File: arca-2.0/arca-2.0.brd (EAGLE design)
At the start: 304.8 x 101.6 mm, 20 parts

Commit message: drivers
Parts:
- added CON_BATTERY, CON_DRV1, CON_DRV2, CON_DRV3, CON_DRV4, CON_DRV5, CON_DRV6: LPTA-2POS, con-phoenix-5mm:8.2X2
- added D10, D5, D6, D7, D8, D9: SS54, diode-ss:SS*
- added D4: (no value), diode:DO201-15
- added DRV_STAT_1, DRV_STAT_2, DRV_STAT_3, DRV_STAT_4, DRV_STAT_5, DRV_STAT_6, FS_STAT_1, FS_STAT_2, FS_STAT_3, FS_STAT_4, FS_STAT_5, FS_STAT_6: (no value), led:CHIPLED_1206
- added FS1, FS2, FS3, FS4, FS5, FS6: 178.6165, fuse-holder-littlefuse:178.6165
- added PWR_12V: RED, led:CHIPLED_1206
- added R10, R13, R16, R19, R22, R7: 10k, rcl:R1206
- added R11, R12, R14, R15, R17, R18, R20, R21, R23, R24, R8, R9: 220, rcl:R1206
- added R6: 300, rcl:R1206
- added SW1: 1101M2S3CQE2, switch-slide:1101M2S3CQE2
- added T1, T2, T3, T4, T5, T6: FQP30N06L, transistor-FQP:TO220V
- C5: value (none) -> 10u
- R1: value 10k -> 68k
- R2: value 1.5k -> 10k
- moved C6 28.4 mm to (289.6, 52.1)
- moved R1 28.4 mm to (284.5, 43.2)
- moved C2 28.4 mm to (289.6, 10.2)
- moved C4 28.4 mm to (289.6, 27.9)
- moved D1 28.4 mm to (284.5, 16.5)
- moved C1 28.4 mm to (269.2, 11.4)
- moved C3 28.4 mm to (269.2, 29.2)
- moved C5 28.4 mm to (269.2, 53.3)
- moved D2 28.4 mm to (284.5, 34.3)
- moved D3 28.4 mm to (284.5, 58.4)
- moved PWR_10V 28.4 mm to (270.5, 59.7)
- moved PWR_3V3 28.4 mm to (270.5, 17.8)
- moved PWR_5V 28.4 mm to (270.5, 35.6)
- moved R2 28.4 mm to (284.5, 40.6)
- moved R3 28.4 mm to (264.2, 17.8)
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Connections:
- new net 12V_CON: CON_BATTERY.1, CON_BATTERY.2, SW1.2
- new net 12V_IN: D4.A, SW1.1
- new net DRV_CTL_1: R7.2, T1.1
- new net DRV_CTL_2: R10.2, T2.1
- new net DRV_CTL_3: R13.2, T3.1
- new net DRV_CTL_4: R16.2, T4.1
- new net DRV_CTL_5: R19.2, T5.1
- new net DRV_CTL_6: R22.2, T6.1
- new net DRV_NEG_1: CON_DRV1.3, CON_DRV1.4, D5.P$2, R9.1, T1.2
- new net DRV_NEG_2: CON_DRV2.3, CON_DRV2.4, D6.P$2, R12.1, T2.2
- new net DRV_NEG_3: CON_DRV3.3, CON_DRV3.4, D7.P$2, R15.1, T3.2
- new net DRV_NEG_4: CON_DRV4.3, CON_DRV4.4, D8.P$2, R18.1, T4.2
- new net DRV_NEG_5: CON_DRV5.3, CON_DRV5.4, D9.P$2, R21.1, T5.2
- new net DRV_NEG_6: CON_DRV6.3, CON_DRV6.4, D10.P$2, R24.1, T6.2
- new net DRV_POS_1: CON_DRV1.1, CON_DRV1.2, D5.P$1, DRV_STAT_1.A, FS1.1, FS1.2, FS1.3, FS1.4, FS_STAT_1.A
- new net DRV_POS_2: CON_DRV2.1, CON_DRV2.2, D6.P$1, DRV_STAT_2.A, FS2.1, FS2.2, FS2.3, FS2.4, FS_STAT_2.A
- new net DRV_POS_3: CON_DRV3.1, CON_DRV3.2, D7.P$1, DRV_STAT_3.A, FS3.1, FS3.2, FS3.3, FS3.4, FS_STAT_3.A
- new net DRV_POS_4: CON_DRV4.1, CON_DRV4.2, D8.P$1, DRV_STAT_4.A, FS4.1, FS4.2, FS4.3, FS4.4, FS_STAT_4.A
- new net DRV_POS_5: CON_DRV5.1, CON_DRV5.2, D9.P$1, DRV_STAT_5.A, FS5.1, FS5.2, FS5.3, FS5.4, FS_STAT_5.A
- new net DRV_POS_6: CON_DRV6.1, CON_DRV6.2, D10.P$1, DRV_STAT_6.A, FS6.1, FS6.2, FS6.3, FS6.4, FS_STAT_6.A
- new net N$1: FS_STAT_2.C, R11.2
- new net N$10: DRV_STAT_3.C, R15.2
- new net N$11: FS_STAT_4.C, R17.2
- new net N$12: DRV_STAT_4.C, R18.2
- new net N$13: FS_STAT_5.C, R20.2
- new net N$14: DRV_STAT_5.C, R21.2
- new net N$15: FS_STAT_6.C, R23.2
- new net N$16: DRV_STAT_6.C, R24.2
- new net N$5: PWR_12V.C, R6.2
- new net N$6: DRV_STAT_2.C, R12.2
- new net N$7: FS_STAT_3.C, R14.2
- new net N$8: FS_STAT_1.C, R8.2
- new net N$9: DRV_STAT_1.C, R9.2
- net +12V: now also D4.C, FS1.5, FS1.6, FS1.7, FS1.8, FS2.5, FS2.6, FS2.7, FS2.8, FS3.5, FS3.6, FS3.7, FS3.8, FS4.5, FS4.6, FS4.7, FS4.8, FS5.5, FS5.6, FS5.7, FS5.8, FS6.5, FS6.6, FS6.7, FS6.8, PWR_12V.A
- net GND: now also CON_BATTERY.3, CON_BATTERY.4, R10.1, R11.1, R13.1, R14.1, R16.1, R17.1, R19.1, R20.1, R22.1, R23.1, R6.1, R7.1, R8.1, T1.3, T2.3, T3.3, T4.3, T5.3, T6.3
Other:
- board text added: "+"
- board text added: "+12V"
- board text added: "-"
- board text added: "GND"

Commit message: started on LC work
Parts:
- added C10, C7, C8, C9: 1u, rcl:C1206
- added C11: 0.1u, rcl:C1206
- added C12, C13, C14, C15: 1n, rcl:C1206
- added CON_LC1, CON_LC2, CON_LC3, CON_LC4: LPTA-4POS, con-phoenix-5mm:8.2X4
- added IC1, IC2, IC3, IC4: MCP6N11R, inamp-microchip:SO-8
- added IC5: LM324D, linear:SO14
- added R25, R29: 39k, rcl:R1206
- added R26, R30: 10k, rcl:R1206
- added R27, R28, R31, R32: 62k, rcl:R1206
- added RF1, RF2, RF3, RF4, RG1, RG2, RG3, RG4: (no value), rcl:R1206
- added RZ1, RZ2, RZ3, RZ4: (no value), pot:S64W
- C6: value (none) -> 10u
- moved D8 240.5 mm to (209.6, 87.6), turned to 270 degrees
- moved R19 239.9 mm to (201.9, 68.6), turned to 180 degrees
- moved R20 229.1 mm to (175.3, 91.4), turned to 270 degrees
- moved R16 229.0 mm to (228.6, 68.6), turned to 180 degrees
- moved R21 227.3 mm to (177.8, 91.4), turned to 270 degrees
- moved T4 223.1 mm to (219.7, 71.1), turned to 90 degrees
- moved DRV_STAT_4 222.1 mm to (204.5, 83.8)
- moved FS4 218.7 mm to (214.6, 67.3), turned to 270 degrees
- moved R17 216.7 mm to (201.9, 90.2), turned to 270 degrees
- moved D9 214.9 mm to (182.9, 87.6), turned to 270 degrees
- moved R18 214.9 mm to (204.5, 90.2), turned to 270 degrees
- moved CON_DRV4 211.9 mm to (217.2, 87.6), turned to 90 degrees
- moved FS_STAT_5 210.4 mm to (175.3, 85.1)
- moved CON_DRV5 208.7 mm to (190.5, 87.6), turned to 90 degrees
- moved R22 206.4 mm to (175.3, 68.6), turned to 180 degrees
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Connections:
- new net LC1+: CON_LC1.3, CON_LC1.4, IC1.3
- new net LC1-: CON_LC1.5, CON_LC1.6, IC1.2
- new net LC1_CAL: C12.2, IC5.1, R25.2
- new net LC1_PREC: IC1.6, R28.1
- new net LC2+: CON_LC2.3, CON_LC2.4, IC2.3
- new net LC2-: CON_LC2.5, CON_LC2.6, IC2.2
- new net LC2_CAL: C14.2, R29.2
- new net LC2_PREC: IC2.6, R32.1
- new net LC3+: CON_LC3.3, CON_LC3.4, IC3.3
- new net LC3-: CON_LC3.5, CON_LC3.6, IC3.2
- new net LC3_PREC: IC3.6
- new net LC4+: CON_LC4.3, CON_LC4.4, IC4.3
- new net LC4-: CON_LC4.5, CON_LC4.6, IC4.2
- new net LC4_PREC: IC4.6
- new net LC_EN: IC1.8, IC2.8, IC3.8, IC4.8
- new net N$17: IC1.5, RF1.1, RG1.2
- new net N$18: IC1.1, RF1.2
- new net N$19: RG1.1, RZ1.S
- new net N$20: IC2.5, RF2.1, RG2.2
- new net N$21: IC2.1, RF2.2
- new net N$22: RG2.1, RZ2.S
- new net N$23: IC3.5, RF3.1, RG3.2
- new net N$24: IC3.1, RF3.2
- new net N$25: RG3.1, RZ3.S
- new net N$26: IC4.5, RF4.1, RG4.2
- new net N$27: IC4.1, RF4.2
- new net N$28: RG4.1, RZ4.S
- new net N$29: IC5.2, R25.1, R26.2
- new net N$30: R29.1, R30.2
- new net N$31: C13.1, IC5.3, R27.2
- new net N$32: C12.1, R27.1, R28.2
- new net N$33: C15.1, R31.2
- new net N$34: C14.1, R31.1, R32.2
- net +10V: now also CON_LC1.1, CON_LC1.2, CON_LC2.1, CON_LC2.2, CON_LC3.1, CON_LC3.2, CON_LC4.1, CON_LC4.2
- net +3V3: now also C10.1, C7.1, C8.1, C9.1, IC1.7, IC2.7, IC3.7, IC4.7, RZ1.E, RZ2.E, RZ3.E, RZ4.E
- net +5V: now also C11.1, IC5.4
- net GND: now also C10.2, C11.2, C13.2, C15.2, C7.2, C8.2, C9.2, CON_LC1.7, CON_LC1.8, CON_LC2.7, CON_LC2.8, CON_LC3.7, CON_LC3.8, CON_LC4.7, CON_LC4.8, IC1.4, IC2.4, IC3.4, IC4.4, IC5.11, R26.1, R30.1, RZ1.A, RZ2.A, RZ3.A, RZ4.A
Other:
- board size 304.8 x 101.6 mm -> 355.6 x 101.6 mm
- board text added: "+10V + - GND"

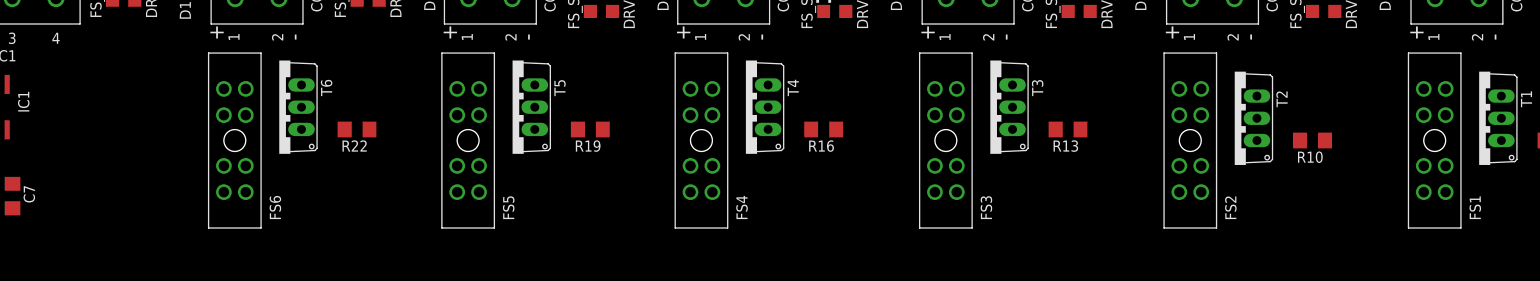
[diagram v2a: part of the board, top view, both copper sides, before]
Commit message: fixed incorrect feedback on LC inamp
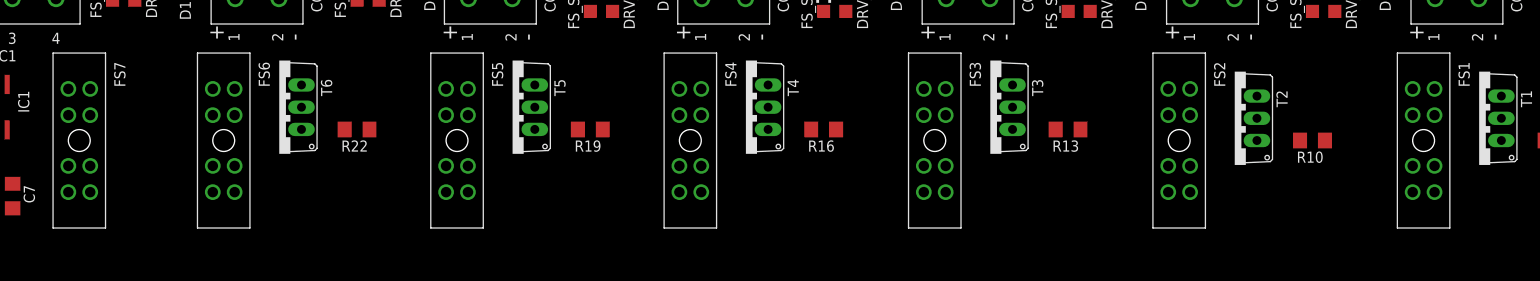
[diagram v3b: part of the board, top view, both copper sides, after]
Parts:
- added FS7: 178.6165, fuse-holder-littlefuse:178.6165
- RF1: value (none) -> 20k
- RG1: value (none) -> 200
- moved FS5 1.27 mm to (186.7, 67.3)
- moved FS1 1.27 mm to (297.2, 67.3)
- moved FS2 1.27 mm to (269.2, 67.3)
- moved FS3 1.27 mm to (241.3, 67.3)
- moved FS4 1.27 mm to (213.4, 67.3)
- moved FS6 1.27 mm to (160.0, 67.3)
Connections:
- removed net N$19: RG1.1, RZ1.S
- removed net N$20: IC2.5, RF2.1, RG2.2
- removed net N$23: IC3.5, RF3.1, RG3.2
- removed net N$26: IC4.5, RF4.1, RG4.2
- new net +10V_FS: CON_LC1.1, CON_LC1.2, CON_LC2.1, CON_LC2.2, CON_LC3.1, CON_LC3.2, CON_LC4.1, CON_LC4.2, FS7.1, FS7.2, FS7.3, FS7.4
- net +10V: now also FS7.5, FS7.6, FS7.7, FS7.8; no longer CON_LC1.1, CON_LC1.2, CON_LC2.1, CON_LC2.2, CON_LC3.1, CON_LC3.2, CON_LC4.1, CON_LC4.2
- net LC1_PREC: now also RF1.1, RG1.2
- net LC2_PREC: now also RF2.1, RG2.2
- net LC3_PREC: now also RF3.1, RG3.2
- net LC4_PREC: now also RF4.1, RG4.2
- net N$17: now also RG1.1, RZ1.S; no longer RF1.1, RG1.2
- net N$22: now also IC2.5
- net N$25: now also IC3.5
- net N$28: now also IC4.5

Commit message: rip 3.3v
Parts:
- removed C1, C2: 10u, rcl:C1206
- removed D1: SS54, diode-ss:SS*
- removed PWR_3V3: RED, led:CHIPLED_1206
- removed VR1: +3.3, LM1084:TO-263-3L
- added C16, C17, C18, C19: 1n, rcl:C1206
- added R33, R37: 39k, rcl:R1206
- added R34, R38: 10k, rcl:R1206
- added R35, R36, R39, R40: 62k, rcl:R1206
- added R41, R42, R43, R44, R45: DNP, rcl:R1206
- R27, R28: value 62k -> 56k
- R3: value 10 -> DNP
- moved R30 126.1 mm to (109.2, 47.0), turned to 270 degrees
- moved R31 118.8 mm to (111.8, 36.8), turned to 180 degrees
- moved C14 115.9 mm to (105.4, 39.4), turned to 180 degrees
- moved R32 115.7 mm to (111.8, 39.4), turned to 180 degrees
- moved C15 114.8 mm to (111.8, 34.3)
- moved R29 108.2 mm to (105.4, 41.9), turned to 180 degrees
- moved R3 53.4 mm to (312.4, 72.4)
- moved R26 21.9 mm to (109.2, 14.0), turned to 90 degrees
- moved R28 17.7 mm to (111.8, 21.6), turned to 180 degrees
- moved R27 16.6 mm to (111.8, 24.1), turned to 180 degrees
- moved C13 16.2 mm to (111.8, 26.7), turned to 0 degrees
- moved R25 13.0 mm to (105.4, 19.1), turned to 180 degrees
- moved C11 12.0 mm to (108.0, 30.5), turned to 0 degrees
- moved C12 10.2 mm to (105.4, 21.6), turned to 180 degrees
- moved IC5 5.39 mm to (100.3, 30.5), turned to 90 degrees
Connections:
- removed net LC_EN: IC1.8, IC2.8, IC3.8, IC4.8
- removed net N$2: PWR_3V3.C, R3.2
- new net LC3_CAL: C16.2, IC5.8, R33.2
- new net LC4_CAL: C18.2, IC5.14, R37.2
- new net N$19: IC5.9, R33.1, R34.2
- new net N$20: C17.1, IC5.10, R35.2
- new net N$23: C16.1, R35.1, R36.2
- new net N$26: IC5.13, R37.1, R38.2
- new net N$35: C19.1, IC5.12, R39.2
- new net N$36: C18.1, R39.1, R40.2
- net +12V: no longer C2.1, D1.P$1, VR1.P$3
- net +3V3: no longer C1.1, C10.1, C7.1, C8.1, C9.1, D1.P$2, IC1.7, IC2.7, IC3.7, IC4.7, PWR_3V3.A, VR1.P$2, VR1.P$4, VR1.P$5
- net +5V: now also C10.1, C7.1, C8.1, C9.1, IC1.7, IC1.8, IC2.7, IC2.8, IC3.7, IC3.8, IC4.7, IC4.8, R3.2, R41.2, R42.2, R43.2, R44.2, R45.2
- net DRV_CTL_1: now also R3.1
- net DRV_CTL_2: now also R41.1
- net DRV_CTL_3: now also R42.1
- net DRV_CTL_4: now also R43.1
- net DRV_CTL_5: now also R44.1
- net DRV_CTL_6: now also R45.1
- net GND: now also C17.2, C19.2, R34.1, R38.1; no longer C1.2, C2.2, R3.1, VR1.P$1
- net LC2_CAL: now also IC5.7
- net LC3_PREC: now also R36.1
- net LC4_PREC: now also R40.1
- net N$30: now also IC5.6
- net N$33: now also IC5.5

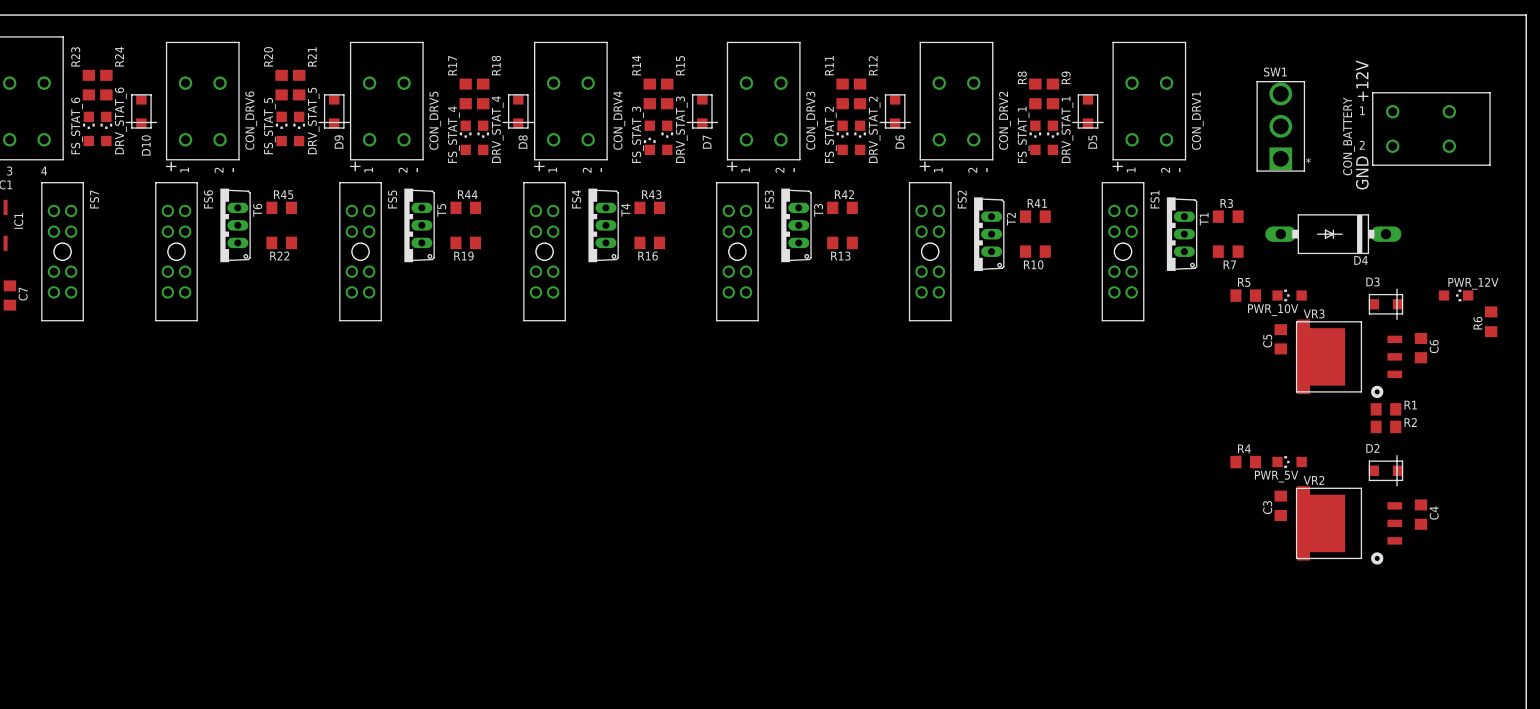
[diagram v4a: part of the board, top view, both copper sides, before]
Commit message: more compact drivers
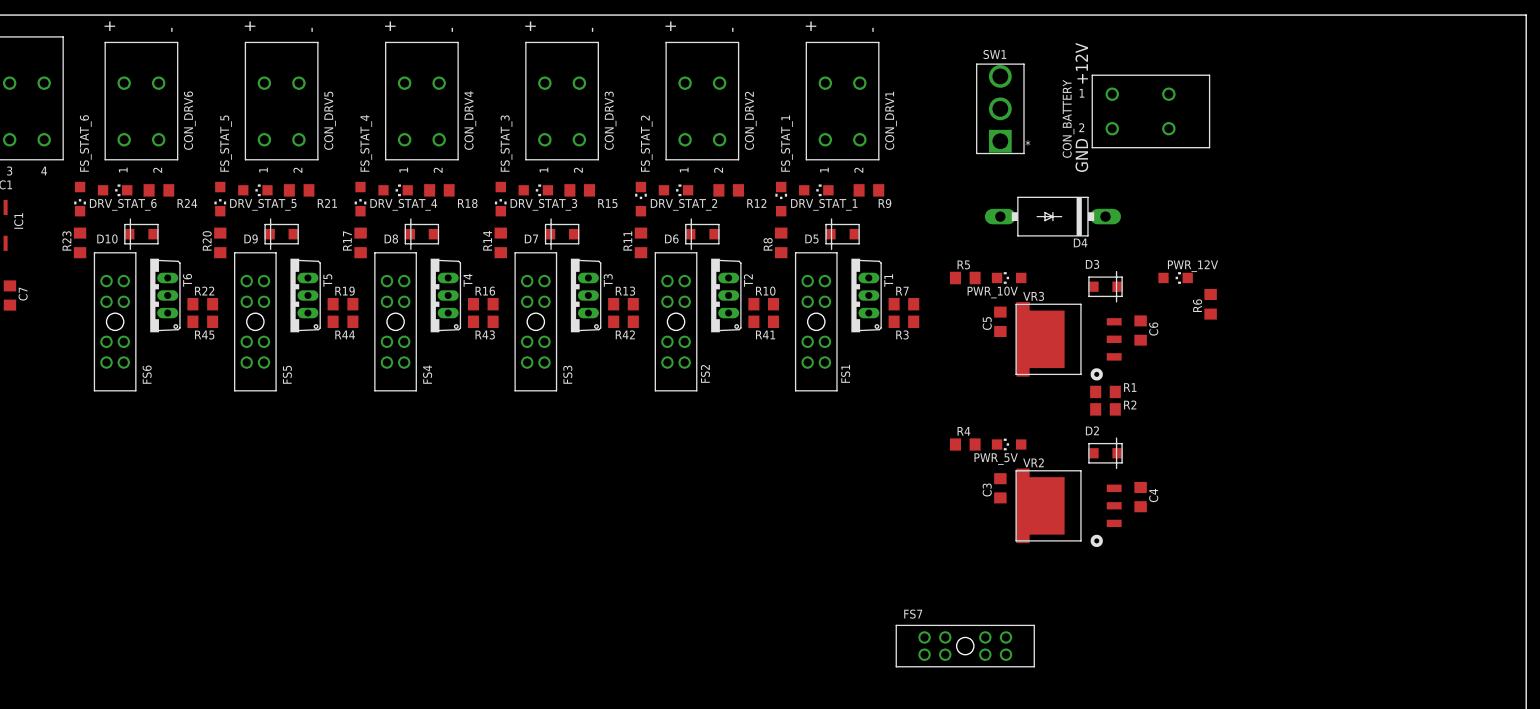
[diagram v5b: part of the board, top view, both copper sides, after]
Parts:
- moved FS7 142.7 mm to (274.3, 10.2), turned to 0 degrees
- moved R3 49.4 mm to (265.4, 57.1)
- moved R7 47.6 mm to (265.4, 59.7)
- moved T1 46.6 mm to (257.8, 61.0)
- moved FS1 45.6 mm to (252.7, 57.1)
- moved CON_DRV1 44.4 mm to (256.5, 87.6)
- moved R8 42.7 mm to (247.7, 68.6), turned to 90 degrees
- moved R41 42.2 mm to (245.1, 57.1)
- moved C3 40.7 mm to (279.4, 33.0)
- moved C5 40.7 mm to (279.4, 57.1)
- moved D4 40.7 mm to (287.0, 72.4)
- moved SW1 40.7 mm to (279.4, 92.7)
- moved C4 40.7 mm to (299.7, 31.8)
- moved C6 40.7 mm to (299.7, 55.9)
- moved CON_BATTERY 40.7 mm to (299.7, 87.6)
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
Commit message: concept for PTs
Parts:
- removed RZ1, RZ2, RZ3, RZ4: (no value), pot:S64W
- added C1, C2: (no value), rcl:C1206
- added C20: 0.1u, rcl:C1206
- added CON_PT1: LPTA-2POS, con-phoenix-5mm:8.2X2
- added IC6: LM324D, linear:SO14
- added R46, R47, R48, R49, R50, R51, R52, R53: 10k, rcl:R1206
- added R54: 220, rcl:R1206
- added R55, R56: (no value), rcl:R1206
- moved FS_STAT_6 74.4 mm to (180.3, 8.89), turned to 270 degrees
- moved R23 72.2 mm to (186.7, 8.89), turned to 180 degrees
- moved CON_DRV6 71.0 mm to (167.6, 17.8), turned to 180 degrees
- moved DRV_STAT_6 68.2 mm to (179.1, 14.0), turned to 0 degrees
- moved FS6 63.8 mm to (198.1, 14.0), turned to 0 degrees
- moved D10 60.3 mm to (185.4, 17.8), turned to 270 degrees
- moved R24 59.9 mm to (179.1, 20.3), turned to 270 degrees
- moved T6 56.6 mm to (194.3, 19.1), turned to 180 degrees
- moved R45 45.9 mm to (198.1, 26.7), turned to 90 degrees
- moved R22 45.8 mm to (195.6, 26.7), turned to 270 degrees
- moved FS7 35.6 mm to (254.0, 39.4)
- moved D4 2.54 mm to (287.0, 74.9)
- moved RF4 1.27 mm to (61.0, 71.1)
- moved RG4 1.27 mm to (61.0, 64.8)
- moved C19 1.27 mm to (88.9, 26.7)
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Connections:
- removed net +3V3: RZ1.E, RZ2.E, RZ3.E, RZ4.E
- removed net N$22: IC2.5, RG2.1, RZ2.S
- new net N$2: IC1.5, R46.1, R47.2, RG1.1
- new net N$37: IC3.5, R50.1, R51.2, RG3.1
- new net N$38: C1.1, IC6.3, R56.2
- new net PT1-: CON_PT1.3, CON_PT1.4, R54.2, R55.1
- new net PT1_CAL: C2.2, IC6.1, IC6.2
- net +10V_FS: now also CON_PT1.1, CON_PT1.2
- net +5V: now also C20.1, IC6.4, R46.2, R48.2, R50.2, R52.2
- net GND: now also C1.2, C20.2, IC6.11, R47.1, R49.1, R51.1, R53.1, R54.1; no longer RZ1.A, RZ2.A, RZ3.A, RZ4.A
- net N$17: now also IC2.5, R48.1, R49.2, RG2.1; no longer IC1.5, RG1.1, RZ1.S
- net N$25: now also C2.1, R55.2, R56.1; no longer IC3.5, RG3.1, RZ3.S
- net N$28: now also R52.1, R53.2; no longer RZ4.S

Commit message: now with 10x gain on PTs
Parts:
- added C21, C22, C23, C24, C25, C26: (no value), rcl:C1206
- added CON_PT2, CON_PT3, CON_PT4: LPTA-2POS, con-phoenix-5mm:8.2X2
- added FS8: 178.6165, fuse-holder-littlefuse:178.6165
- added R57, R60, R63: 22, rcl:R1206
- added R58, R59, R61, R62, R64, R65: (no value), rcl:R1206
- added R66, R68, R70, R72: 47k, rcl:R1206
- added R67, R69, R71, R73: 5.1k, rcl:R1206
- R54: value 220 -> 22
- RF2, RF3, RF4: value (none) -> 20k
- RG2, RG3, RG4: value (none) -> 200
- moved FS7 207.3 mm to (48.3, 64.8), turned to 270 degrees
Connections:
- new net +5V_FS: CON_LC1.1, CON_LC1.2, CON_LC2.1, CON_LC2.2, CON_LC3.1, CON_LC3.2, CON_LC4.1, CON_LC4.2, FS8.1, FS8.2, FS8.3, FS8.4
- new net N$22: C22.1, R58.2, R59.1
- new net N$39: C21.1, IC6.5, R59.2
- new net N$40: C24.1, R61.2, R62.1
- new net N$41: C23.1, IC6.10, R62.2
- new net N$42: C26.1, R64.2, R65.1
- new net N$43: C25.1, IC6.12, R65.2
- new net N$44: IC6.13, R72.1, R73.2
- new net N$45: IC6.9, R70.1, R71.2
- new net N$46: IC6.6, R68.1, R69.2
- new net N$47: IC6.2, R66.1, R67.2
- new net PT2-: CON_PT2.3, CON_PT2.4, R57.2, R58.1
- new net PT2_CAL: C22.2, IC6.7, R68.2
- new net PT3-: CON_PT3.3, CON_PT3.4, R60.2, R61.1
- new net PT3_CAL: C24.2, IC6.8, R70.2
- new net PT4-: CON_PT4.3, CON_PT4.4, R63.2, R64.1
- new net PT4_CAL: C26.2, IC6.14, R72.2
- net +10V_FS: now also CON_PT2.1, CON_PT2.2, CON_PT3.1, CON_PT3.2, CON_PT4.1, CON_PT4.2; no longer CON_LC1.1, CON_LC1.2, CON_LC2.1, CON_LC2.2, CON_LC3.1, CON_LC3.2, CON_LC4.1, CON_LC4.2
- net +5V: now also FS8.5, FS8.6, FS8.7, FS8.8
- net GND: now also C21.2, C23.2, C25.2, R57.1, R60.1, R63.1, R67.1, R69.1, R71.1, R73.1
- net PT1_CAL: now also R66.2; no longer IC6.2

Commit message: board relay concept
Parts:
- moved C3 49.5 mm to (328.9, 33.0)
- moved C5 49.5 mm to (328.9, 57.1)
- moved D2 49.5 mm to (344.2, 38.1)
- moved D3 49.5 mm to (344.2, 62.2)
- moved D4 49.5 mm to (336.6, 74.9)
- moved FS_STAT_3 49.5 mm to (256.5, 74.9)
- moved R1 49.5 mm to (344.2, 47.0)
- moved R14 49.5 mm to (256.5, 68.6)
- moved R15 49.5 mm to (268.0, 76.2)
- moved R2 49.5 mm to (344.2, 44.5)
- moved R4 49.5 mm to (323.9, 39.4)
- moved R5 49.5 mm to (323.9, 63.5)
- moved R6 49.5 mm to (359.4, 59.7)
- moved SW1 49.5 mm to (328.9, 92.7)
- moved CON_DRV2 49.5 mm to (285.8, 87.6)
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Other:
- board size 355.6 x 101.6 mm -> 405.1 x 101.6 mm
- board text added: "+5V + - GND"
- board text removed: "+10V + - GND"
